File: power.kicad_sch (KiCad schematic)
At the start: 46 parts, among them J25 Conn_01x02, U1 TLV75733PDBV, U2 TPS56A37, U7 TPS56A37

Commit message: schem: add battery holder footprint
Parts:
- BT1: footprint (none) -> GLCS:Power battery holder
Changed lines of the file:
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@@
 			)
 		)
-		(property "Footprint" ""
+		(property "Footprint" "GLCS:Power battery holder"
 			(at 26.67 116.586 90)
 			(effects

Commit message: schem: add sheet title
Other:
- company: (none) -> Valrobotik
- title: (none) -> Carte alim CDF 1
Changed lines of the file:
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@@
 	(generator_version "9.0")
 	(paper "A4")
+	(title_block
+		(title "Carte alim CDF 1")
+		(date "2026-01-15")
+		(rev "01")
+		(company "Valrobotik")
+	)
 	(rectangle
 		(start 106.68 29.21)

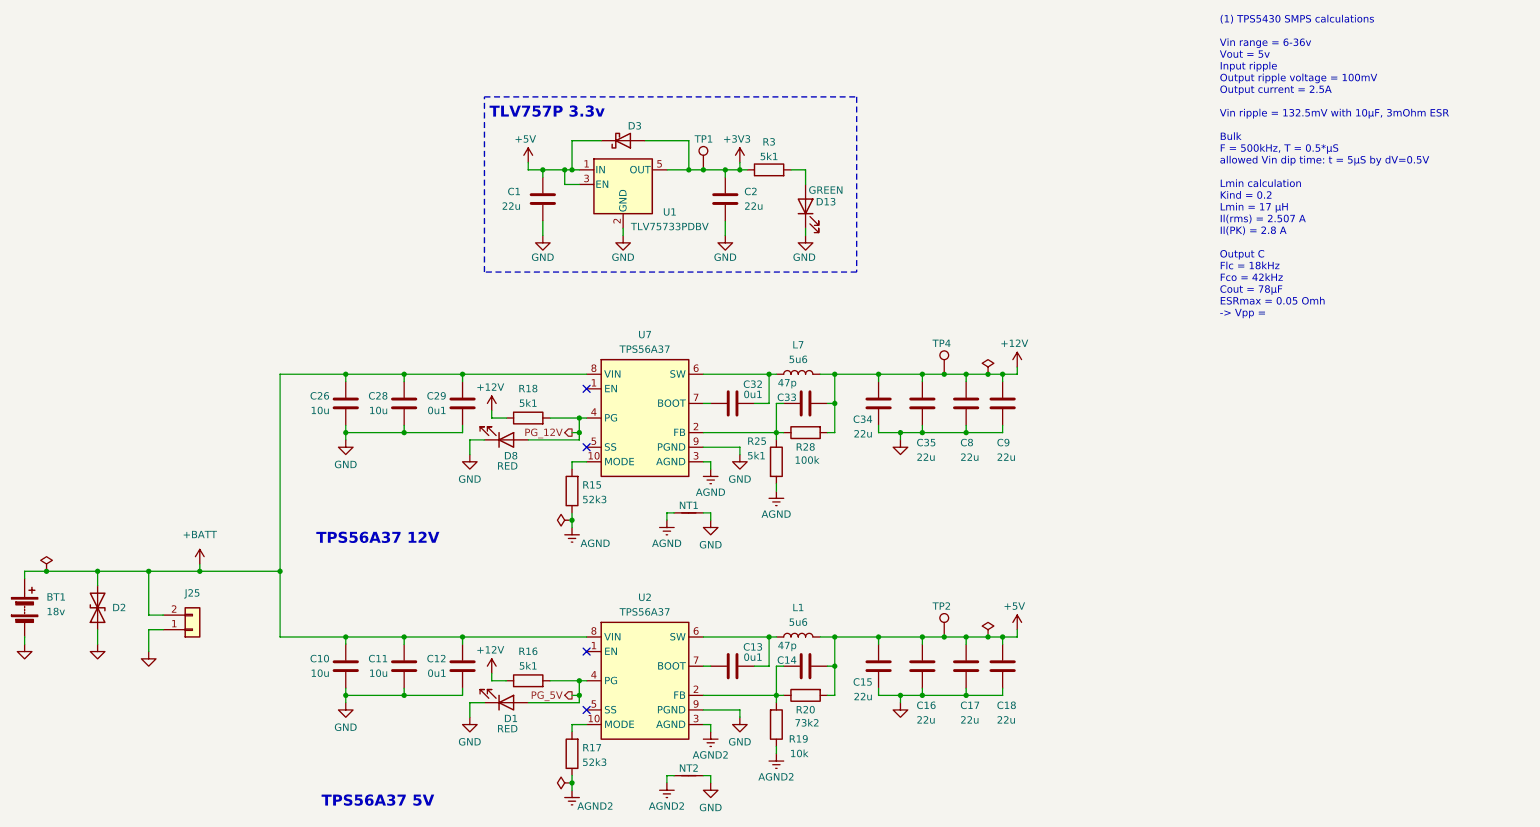
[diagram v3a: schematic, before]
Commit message: schem: renumber
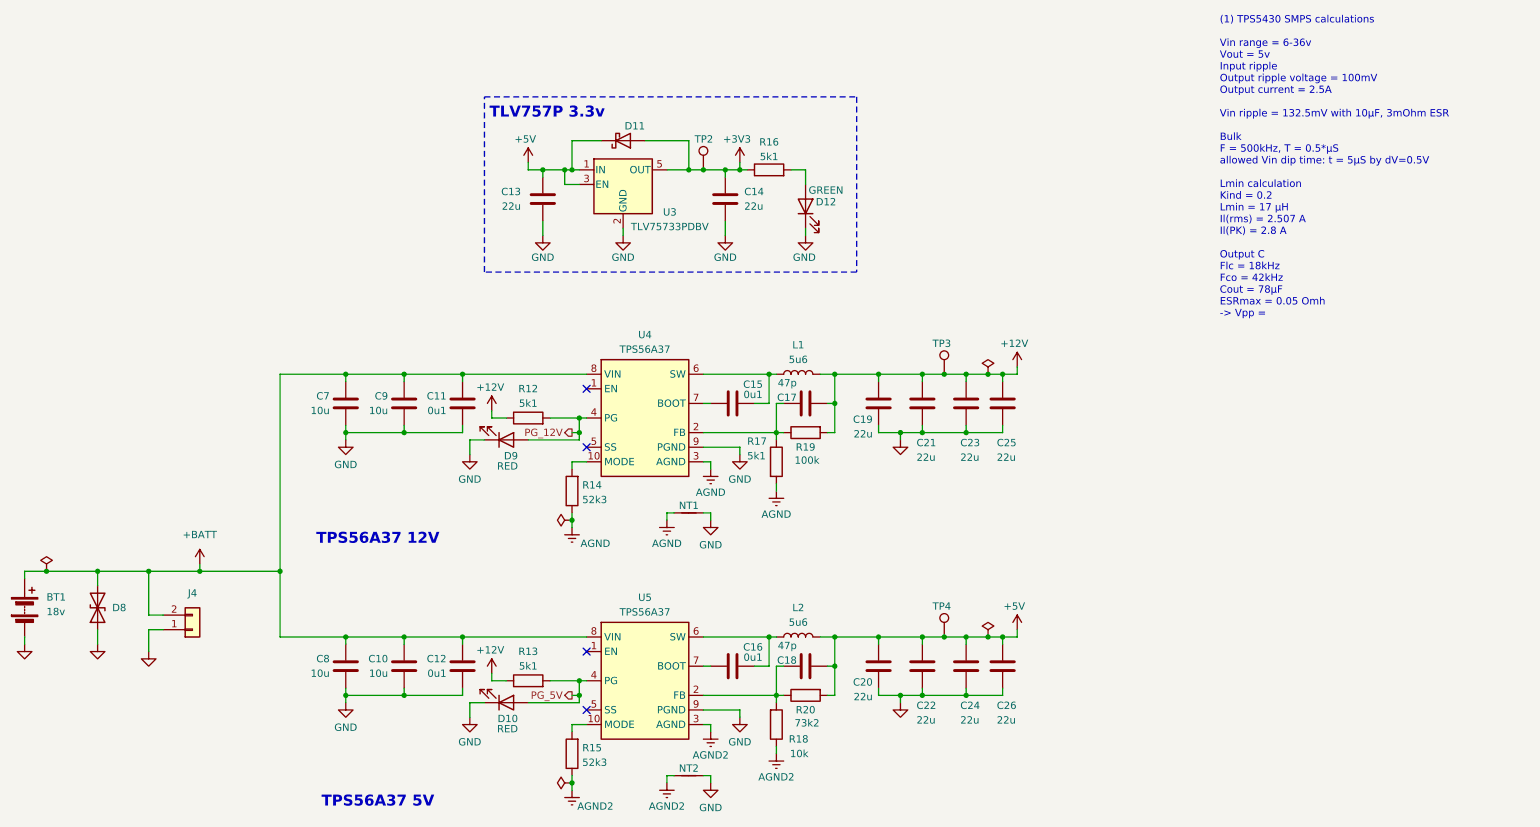
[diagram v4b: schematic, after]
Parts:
- renumbered C11 to C10, C29 to C11, C1 to C13, C2 to C14, C32 to C15, C13 to C16, C33 to C17, C14 to C18, C34 to C19, C15 to C20, C35 to C21, C16 to C22, C8 to C23, C17 to C24, C9 to C25, C18 to C26, C26 to C7, C10 to C8, C28 to C9, D1 to D10, D3 to D11, D13 to D12, D2 to D8, D8 to D9, J25 to J4, L7 to L1, L1 to L2, R18 to R12, R16 to R13, R15 to R14, R17 to R15, R3 to R16, R25 to R17, R19 to R18, R28 to R19, TP1 to TP2, TP4 to TP3, TP2 to TP4, U1 to U3, U7 to U4, U2 to U5

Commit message: pcb: add smps layout
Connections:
- net +12V: no longer R12.1, R13.1
- net +3V3: now also R12.1, R13.1
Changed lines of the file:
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@@
 	)
 	(symbol
-		(lib_id "power:+12V")
-		(at 107.95 129.54 0)
-		(unit 1)
-		(exclude_from_sim no)
-		(in_bom yes)
-		(on_board yes)
-		(dnp no)
-		(property "Reference" "#PWR035"
-			(at 107.95 133.35 0)
-			(effects
-				(font
-					(size 1.27 1.27)
-				)
-				(hide yes)
-			)
-		)
-		(property "Value" "+12V"
-			(at 107.696 125.476 0)
-			(effects
-				(font
-					(size 1.27 1.27)
-				)
-			)
-		)
-		(property "Footprint" ""
-			(at 107.95 129.54 0)
-			(effects
-				(font
-					(size 1.27 1.27)
-				)
-				(hide yes)
-			)
-		)
-		(property "Datasheet" ""
-			(at 107.95 129.54 0)
-			(effects
-				(font
-					(size 1.27 1.27)
-				)
-				(hide yes)
-			)
-		)
-		(property "Description" "Power symbol creates a global label with name \"+12V\""
-			(at 107.95 129.54 0)
-			(effects
-				(font
-					(size 1.27 1.27)
-				)
-				(hide yes)
-			)
-		)
-		(pin "1"
-		)
-		(instances
-			(project "valrob-carte-alim-cdf-1"
-				(path "/8d7b287d-627f-46aa-8c27-0b5ed29ab4a2/0cc01053-a223-4e8e-b0aa-a1ec618db290"
-					(reference "#PWR035")
-					(unit 1)
-				)
-			)
-		)
-	)
-	(symbol
 		(lib_id "power:GND")
 		(at 104.14 137.16 0)
@@
 	)
 	(symbol
-		(lib_id "power:+12V")
-		(at 107.95 83.82 0)
-		(unit 1)
-		(exclude_from_sim no)
-		(in_bom yes)
-		(on_board yes)
-		(dnp no)
-		(property "Reference" "#PWR034"
-			(at 107.95 87.63 0)
-			(effects
-				(font
-					(size 1.27 1.27)
-				)
-				(hide yes)
-			)
-		)
-		(property "Value" "+12V"
-			(at 107.696 79.756 0)
-			(effects
-				(font
-					(size 1.27 1.27)
-				)
-			)
-		)
-		(property "Footprint" ""
-			(at 107.95 83.82 0)
-			(effects
-				(font
-					(size 1.27 1.27)
-				)
-				(hide yes)
-			)
-		)
-		(property "Datasheet" ""
-			(at 107.95 83.82 0)
-			(effects
-				(font
-					(size 1.27 1.27)
-				)
-				(hide yes)
-			)
-		)
-		(property "Description" "Power symbol creates a global label with name \"+12V\""
-			(at 107.95 83.82 0)
-			(effects
-				(font
-					(size 1.27 1.27)
-				)
-				(hide yes)
-			)
-		)
-		(pin "1"
-		)
-		(instances
-			(project "valrob-carte-alim-cdf-1"
-				(path "/8d7b287d-627f-46aa-8c27-0b5ed29ab4a2/0cc01053-a223-4e8e-b0aa-a1ec618db290"
-					(reference "#PWR034")
-					(unit 1)
-				)
-			)
-		)
-	)
-	(symbol
 		(lib_id "Device:C")
 		(at 116.84 46.99 0)
@@
 	)
 	(symbol
+		(lib_id "power:+3V3")
+		(at 107.95 129.54 0)
+		(unit 1)
+		(exclude_from_sim no)
+		(in_bom yes)
+		(on_board yes)
+		(dnp no)
+		(fields_autoplaced yes)
+		(property "Reference" "#PWR035"
+			(at 107.95 133.35 0)
+			(effects
+				(font
+					(size 1.27 1.27)
+				)
+				(hide yes)
+			)
+		)
+		(property "Value" "+3V3"
+			(at 107.442 125.476 0)
+			(effects
+				(font
+					(size 1.27 1.27)
+				)
+			)
+		)
+		(property "Footprint" ""
+			(at 107.95 129.54 0)
+			(effects
+				(font
+					(size 1.27 1.27)
+				)
+				(hide yes)
+			)
+		)
+		(property "Datasheet" ""
+			(at 107.95 129.54 0)
+			(effects
+				(font
+					(size 1.27 1.27)
+				)
+				(hide yes)
+			)
+		)
+		(property "Description" "Power symbol creates a global label with name \"+3V3\""
+			(at 107.95 129.54 0)
+			(effects
+				(font
+					(size 1.27 1.27)
+				)
+				(hide yes)
+			)
+		)
+		(pin "1"
+		)
+		(instances
+			(project "valrob-carte-alim-cdf-1"
+				(path "/8d7b287d-627f-46aa-8c27-0b5ed29ab4a2/0cc01053-a223-4e8e-b0aa-a1ec618db290"
+					(reference "#PWR035")
+					(unit 1)
+				)
+			)
+		)
+	)
+	(symbol
 		(lib_id "Device:C")
 		(at 182.88 128.27 0)
@@
 					(unit 1)
 				)
+			)
+		)
+	)
+	(symbol
+		(lib_id "power:+3V3")
+		(at 107.95 83.82 0)
+		(unit 1)
+		(exclude_from_sim no)
+		(in_bom yes)
+		(on_board yes)
+		(dnp no)
+		(fields_autoplaced yes)
+		(property "Reference" "#PWR034"
+			(at 107.95 87.63 0)
+			(effects
+				(font
+					(size 1.27 1.27)
+				)
+				(hide yes)
+			)
+		)
+		(property "Value" "+3V3"
+			(at 107.442 79.756 0)
+			(effects
+				(font
+					(size 1.27 1.27)
+				)
+			)
+		)
+		(property "Footprint" ""
+			(at 107.95 83.82 0)
+			(effects
+				(font
+					(size 1.27 1.27)
+				)
+				(hide yes)
+			)
+		)
+		(property "Datasheet" ""
+			(at 107.95 83.82 0)
+			(effects
+				(font
+					(size 1.27 1.27)
+				)
+				(hide yes)
+			)
+		)
+		(property "Description" "Power symbol creates a global label with name \"+3V3\""
+			(at 107.95 83.82 0)
+			(effects
+				(font
+					(size 1.27 1.27)
+				)
+				(hide yes)
+			)
+		)
+		(pin "1"
+		)
+		(instances
+			(project "valrob-carte-alim-cdf-1"
+				(path "/8d7b287d-627f-46aa-8c27-0b5ed29ab4a2/0cc01053-a223-4e8e-b0aa-a1ec618db290"
+					(reference "#PWR034")
+					(unit 1)
+				)

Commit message: schem: add general EN jumper
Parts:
- added JP10: Jumper_2_Small_Open, Connector_PinHeader_2.54mm:PinHeader_2x01_P2.54mm_Vertical, symbol Jumper:Jumper_2_Open
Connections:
- net GND: now also JP10.2 (B)
- net EN: now reaches U5.1 (EN)
- net EN: now also U4.1 (EN), JP10.1 (A)
- no-connect marks 4 -> 2
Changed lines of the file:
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@@
 	)
 	(no_connect
-		(at 124.46 125.73)
-	)
-	(no_connect
-		(at 124.46 80.01)
-	)
-	(no_connect
 		(at 124.46 135.89)
 	)
@@
 	(wire
 		(pts
+			(xy 120.65 125.73) (xy 124.46 125.73)
+		)
+		(stroke
+			(width 0)
+			(type default)
+		)
+	)
+	(wire
+		(pts
 			(xy 144.78 123.19) (xy 156.21 123.19)
 		)
@@
 	(wire
 		(pts
+			(xy 120.65 80.01) (xy 124.46 80.01)
+		)
+		(stroke
+			(width 0)
+			(type default)
+		)
+	)
+	(wire
+		(pts
 			(xy 162.56 41.91) (xy 162.56 44.45)
 		)
@@
 	(wire
 		(pts
+			(xy 54.61 91.44) (xy 55.88 91.44)
+		)
+		(stroke
+			(width 0)
+			(type default)
+		)
+	)
+	(wire
+		(pts
 			(xy 82.55 123.19) (xy 82.55 124.46)
 		)
@@
 	(wire
 		(pts
+			(xy 55.88 91.44) (xy 55.88 92.71)
+		)
+		(stroke
+			(width 0)
+			(type default)
+		)
+	)
+	(wire
+		(pts
 			(xy 26.67 123.19) (xy 26.67 124.46)
 		)
@@
 	(wire
 		(pts
+			(xy 40.64 91.44) (xy 44.45 91.44)
+		)
+		(stroke
+			(width 0)
+			(type default)
+		)
+	)
+	(wire
+		(pts
 			(xy 82.55 77.47) (xy 82.55 78.74)
 		)
@@
 		)
 	)
+	(label "EN"
+		(at 40.64 91.44 0)
+		(effects
+			(font
+				(size 1.27 1.27)
+			)
+			(justify left bottom)
+		)
+	)
+	(label "EN"
+		(at 120.65 80.01 0)
+		(effects
+			(font
+				(size 1.27 1.27)
+			)
+			(justify left bottom)
+		)
+	)
+	(label "EN"
+		(at 120.65 125.73 0)
+		(effects
+			(font
+				(size 1.27 1.27)
+			)
+			(justify left bottom)
+		)
+	)
 	(hierarchical_label "PG_12V"
 		(shape output)
@@
 	)
 	(symbol
+		(lib_id "power:GND")
+		(at 55.88 92.71 0)
+		(unit 1)
+		(exclude_from_sim no)
+		(in_bom yes)
+		(on_board yes)
+		(dnp no)
+		(fields_autoplaced yes)
+		(property "Reference" "#PWR074"
+			(at 55.88 99.06 0)
+			(effects
+				(font
+					(size 1.27 1.27)
+				)
+				(hide yes)
+			)
+		)
+		(property "Value" "GND"
+			(at 55.88 97.79 0)
+			(effects
+				(font
+					(size 1.27 1.27)
+				)
+				(hide yes)
+			)
+		)
+		(property "Footprint" ""
+			(at 55.88 92.71 0)
+			(effects
+				(font
+					(size 1.27 1.27)
+				)
+				(hide yes)
+			)
+		)
+		(property "Datasheet" ""
+			(at 55.88 92.71 0)
+			(effects
+				(font
+					(size 1.27 1.27)
+				)
+				(hide yes)
+			)
+		)
+		(property "Description" "Power symbol creates a global label with name \"GND\" , ground"
+			(at 55.88 92.71 0)
+			(effects
+				(font
+					(size 1.27 1.27)
+				)
+				(hide yes)
+			)
+		)
+		(pin "1"
+		)
+		(instances
+			(project "valrob-carte-alim-cdf-1"
+				(path "/8d7b287d-627f-46aa-8c27-0b5ed29ab4a2/0cc01053-a223-4e8e-b0aa-a1ec618db290"
+					(reference "#PWR074")
+					(unit 1)
+				)
+			)
+		)
+	)
+	(symbol
 		(lib_id "Device:C")
 		(at 82.55 82.55 0)
@@
 					(unit 1)
 				)
+			)
+		)
+	)
+	(symbol
+		(lib_id "Jumper:Jumper_2_Open")
+		(at 49.53 91.44 0)
+		(unit 1)
+		(exclude_from_sim no)
+		(in_bom yes)
+		(on_board yes)
+		(dnp no)
+		(fields_autoplaced yes)
+		(property "Reference" "JP10"
+			(at 49.53 87.63 0)
+			(effects
+				(font
+					(size 1.27 1.27)
+				)
+			)
+		)
+		(property "Value" "Jumper_2_Small_Open"
+			(at 49.53 87.63 0)
+			(effects
+				(font
+					(size 1.27 1.27)
+				)
+				(hide yes)
+			)
+		)
+		(property "Footprint" "Connector_PinHeader_2.54mm:PinHeader_2x01_P2.54mm_Vertical"
+			(at 49.53 91.44 0)
+			(effects
+				(font
+					(size 1.27 1.27)
+				)
+				(hide yes)
+			)
+		)
+		(property "Datasheet" "~"
+			(at 49.53 91.44 0)
+			(effects
+				(font
+					(size 1.27 1.27)
+				)
+				(hide yes)
+			)
+		)
+		(property "Description" "Jumper, 2-pole, open"
+			(at 49.53 91.44 0)
+			(effects
+				(font
+					(size 1.27 1.27)
+				)
+				(hide yes)
+			)
+		)
+		(pin "2"
+		)
+		(pin "1"
+		)
+		(instances
+			(project "valrob-carte-alim-cdf-1"
+				(path "/8d7b287d-627f-46aa-8c27-0b5ed29ab4a2/0cc01053-a223-4e8e-b0aa-a1ec618db290"
+					(reference "JP10")
+					(unit 1)
+				)
